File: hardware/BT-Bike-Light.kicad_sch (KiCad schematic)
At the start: 19 parts, among them J1 Conn_ARM_JTAG_SWD_10, U1 BC805M, U2 LIS2DTW12, U3 PAM2808

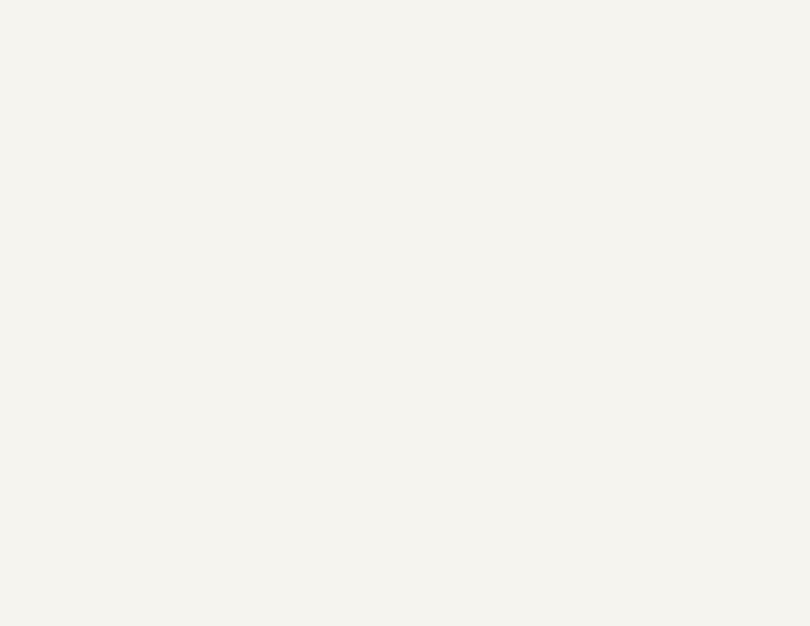
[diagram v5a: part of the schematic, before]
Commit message: Add USB-C receptacle
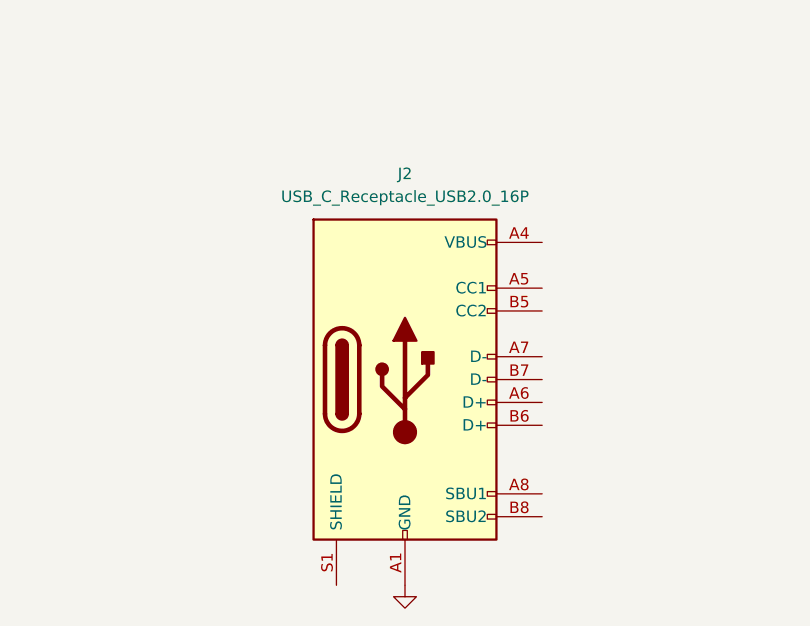
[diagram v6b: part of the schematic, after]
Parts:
- added J2: USB_C_Receptacle_USB2.0_16P, GCT:USB_C_Receptacle_GCT_USB4145, symbol Connector:USB_C_Receptacle_USB2.0_16P
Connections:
- net GND: now also J2.A1 (GND), J2.A12 (GND), J2.B1 (GND), J2.B12 (GND)
- new net: J2.A4 (VBUS), J2.A9 (VBUS), J2.B4 (VBUS), J2.B9 (VBUS)
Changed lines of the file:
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@@
+	)
+	(symbol
+		(lib_id "power:GND")
+		(at 87.63 182.88 0)
+		(unit 1)
+		(exclude_from_sim no)
+		(in_bom yes)
+		(on_board yes)
+		(dnp no)
+		(fields_autoplaced yes)
+		(property "Reference" "#PWR014"
+			(at 87.63 189.23 0)
+			(effects
+				(font
+					(size 1.27 1.27)
+				)
+				(hide yes)
+			)
+		)
+		(property "Value" "GND"
+			(at 87.63 187.96 0)
+			(effects
+				(font
+					(size 1.27 1.27)
+				)
+				(hide yes)
+			)
+		)
+		(property "Footprint" ""
+			(at 87.63 182.88 0)
+			(effects
+				(font
+					(size 1.27 1.27)
+				)
+				(hide yes)
+			)
+		)
+		(property "Datasheet" ""
+			(at 87.63 182.88 0)
+			(effects
+				(font
+					(size 1.27 1.27)
+				)
+				(hide yes)
+			)
+		)
+		(property "Description" "Power symbol creates a global label with name \"GND\" , ground"
+			(at 87.63 182.88 0)
+			(effects
+				(font
+					(size 1.27 1.27)
+				)
+				(hide yes)
+			)
+		)
+		(pin "1"
+		)
+		(instances
+			(project "BT-Bike-Light"
+				(path "/3263b444-391f-435a-aeab-6f7fca8830e2"
+					(reference "#PWR014")
+					(unit 1)
+				)
+			)
+		)
 	)
 	(symbol
@@
 					(unit 1)
 				)
+			)
+		)
+	)
+	(symbol
+		(lib_id "Connector:USB_C_Receptacle_USB2.0_16P")
+		(at 87.63 160.02 0)
+		(unit 1)
+		(exclude_from_sim no)
+		(in_bom yes)
+		(on_board yes)
+		(dnp no)
+		(fields_autoplaced yes)
+		(property "Reference" "J2"
+			(at 87.63 137.16 0)
+			(effects
+				(font
+					(size 1.27 1.27)
+				)
+			)
+		)
+		(property "Value" "USB_C_Receptacle_USB2.0_16P"
+			(at 87.63 139.7 0)
+			(effects
+				(font
+					(size 1.27 1.27)
+				)
+			)
+		)
+		(property "Footprint" "GCT:USB_C_Receptacle_GCT_USB4145"
+			(at 91.44 160.02 0)
+			(effects
+				(font
+					(size 1.27 1.27)
+				)
+				(hide yes)
+			)
+		)
+		(property "Datasheet" "https://www.usb.org/sites/default/files/documents/usb_type-c.zip"
+			(at 91.44 160.02 0)
+			(effects
+				(font
+					(size 1.27 1.27)
+				)
+				(hide yes)
+			)
+		)
+		(property "Description" "USB 2.0-only 16P Type-C Receptacle connector"
+			(at 87.63 160.02 0)
+			(effects
+				(font
+					(size 1.27 1.27)
+				)
+				(hide yes)
+			)
+		)
+		(pin "A12"
+		)
+		(pin "A6"
+		)
+		(pin "A8"
+		)
+		(pin "S1"
+		)
+		(pin "A4"
+		)
+		(pin "A7"
+		)
+		(pin "A5"
+		)
+		(pin "B8"
+		)
+		(pin "B7"
+		)
+		(pin "B9"
+		)
+		(pin "B1"
+		)
+		(pin "A1"
+		)
+		(pin "B6"
+		)
+		(pin "B5"
+		)
+		(pin "A9"
+		)
+		(pin "B4"
+		)
+		(pin "B12"
+		)
+		(instances
+			(project ""
+				(path "/3263b444-391f-435a-aeab-6f7fca8830e2"
+					(reference "J2")
+					(unit 1)
+				)

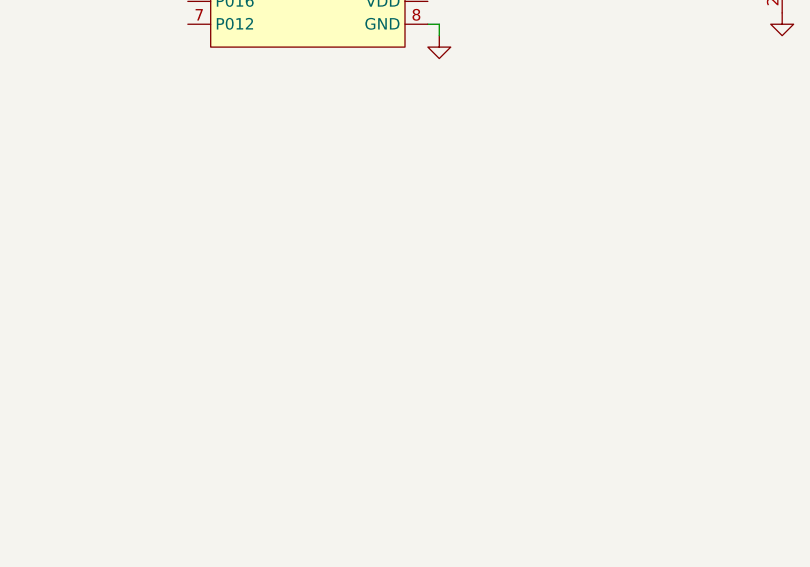
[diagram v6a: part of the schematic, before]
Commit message: Add button
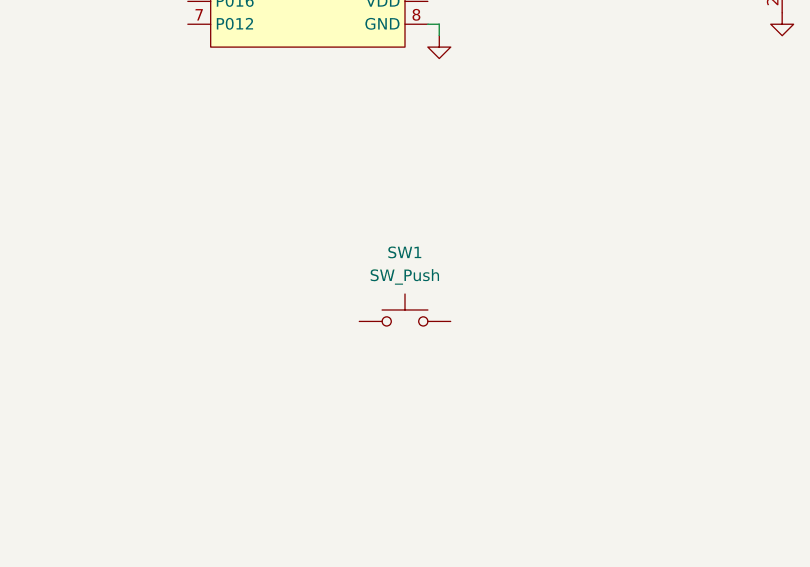
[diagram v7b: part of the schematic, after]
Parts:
- added SW1: SW_Push, Button_Switch_THT:SW_Tactile_SPST_Angled_PTS645Vx58-2LFS, symbol Switch:SW_Push
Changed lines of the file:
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@@
+	)
+	(symbol
+		(lib_id "Switch:SW_Push")
+		(at 151.13 140.97 0)
+		(unit 1)
+		(exclude_from_sim no)
+		(in_bom yes)
+		(on_board yes)
+		(dnp no)
+		(fields_autoplaced yes)
+		(property "Reference" "SW1"
+			(at 151.13 133.35 0)
+			(effects
+				(font
+					(size 1.27 1.27)
+				)
+			)
+		)
+		(property "Value" "SW_Push"
+			(at 151.13 135.89 0)
+			(effects
+				(font
+					(size 1.27 1.27)
+				)
+			)
+		)
+		(property "Footprint" "Button_Switch_THT:SW_Tactile_SPST_Angled_PTS645Vx58-2LFS"
+			(at 151.13 135.89 0)
+			(effects
+				(font
+					(size 1.27 1.27)
+				)
+				(hide yes)
+			)
+		)
+		(property "Datasheet" "https://www.ckswitches.com/media/1471/pts645.pdf"
+			(at 151.13 135.89 0)
+			(effects
+				(font
+					(size 1.27 1.27)
+				)
+				(hide yes)
+			)
+		)
+		(property "Description" "Push button switch, generic, two pins"
+			(at 151.13 140.97 0)
+			(effects
+				(font
+					(size 1.27 1.27)
+				)
+				(hide yes)
+			)
+		)
+		(pin "2"
+		)
+		(pin "1"
+		)
+		(instances
+			(project ""
+				(path "/3263b444-391f-435a-aeab-6f7fca8830e2"
+					(reference "SW1")
+					(unit 1)
+				)
+			)
+		)
 	)
 	(symbol

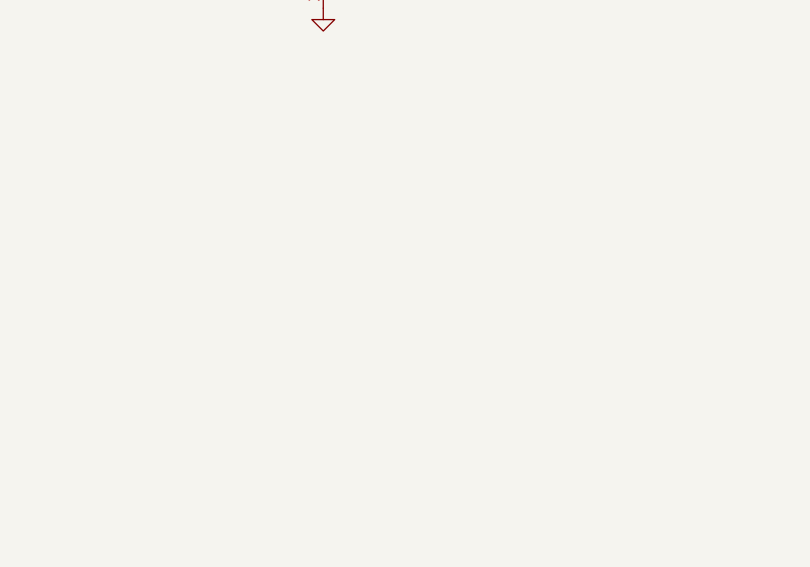
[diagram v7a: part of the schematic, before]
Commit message: Add buzzer
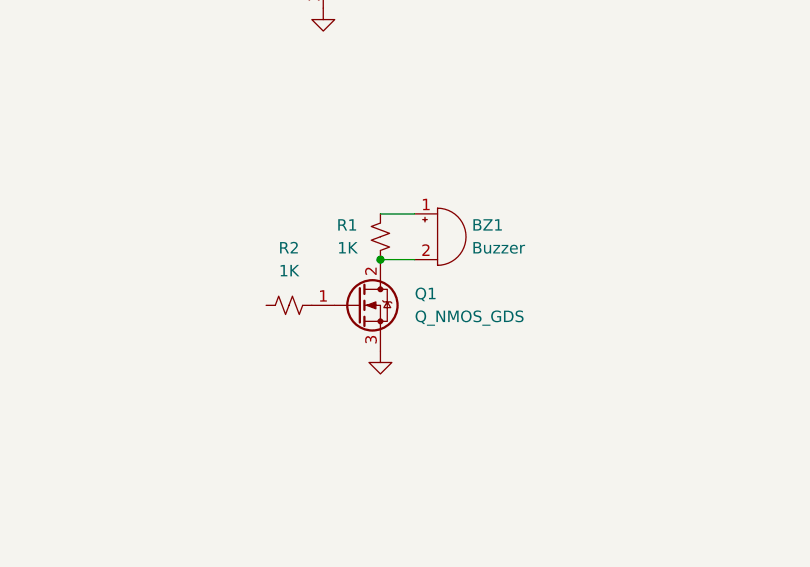
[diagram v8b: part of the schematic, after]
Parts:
- added BZ1: Buzzer, PUI-Audio:PUI_AT-1220-TT-3V-2-R, symbol Device:Buzzer
- added Q1: Q_NMOS_GDS, symbol Device:Q_NMOS_GDS
- added R1, R2: 1K, symbol Device:R_Small_US
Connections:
- net GND: now also Q1.3 (S)
- new net: Q1.1 (G), R2.2
- new net: BZ1.2 (-), Q1.2 (D), R1.2
- new net: BZ1.1 (+), R1.1
